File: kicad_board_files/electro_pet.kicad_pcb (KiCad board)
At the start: 2 copper layers, 42 x 63.8 mm, 20 parts, among them M3_bolt_nut_custom VAL**, SW1 SWITCH_INV, SW2 SW_PUSH, SW3 SW_PUSH, U1 8X8_LED_MATRIX, U2 LIPO_CHARGER, U3 ELECTRO_HAT, U4 V_REG, U5 MPU-6050, U6 DC_DC_BOOST, U7 ARDUINO_PRO_MICRO, U8 BATTERY_CUSTOM, U9 A3144

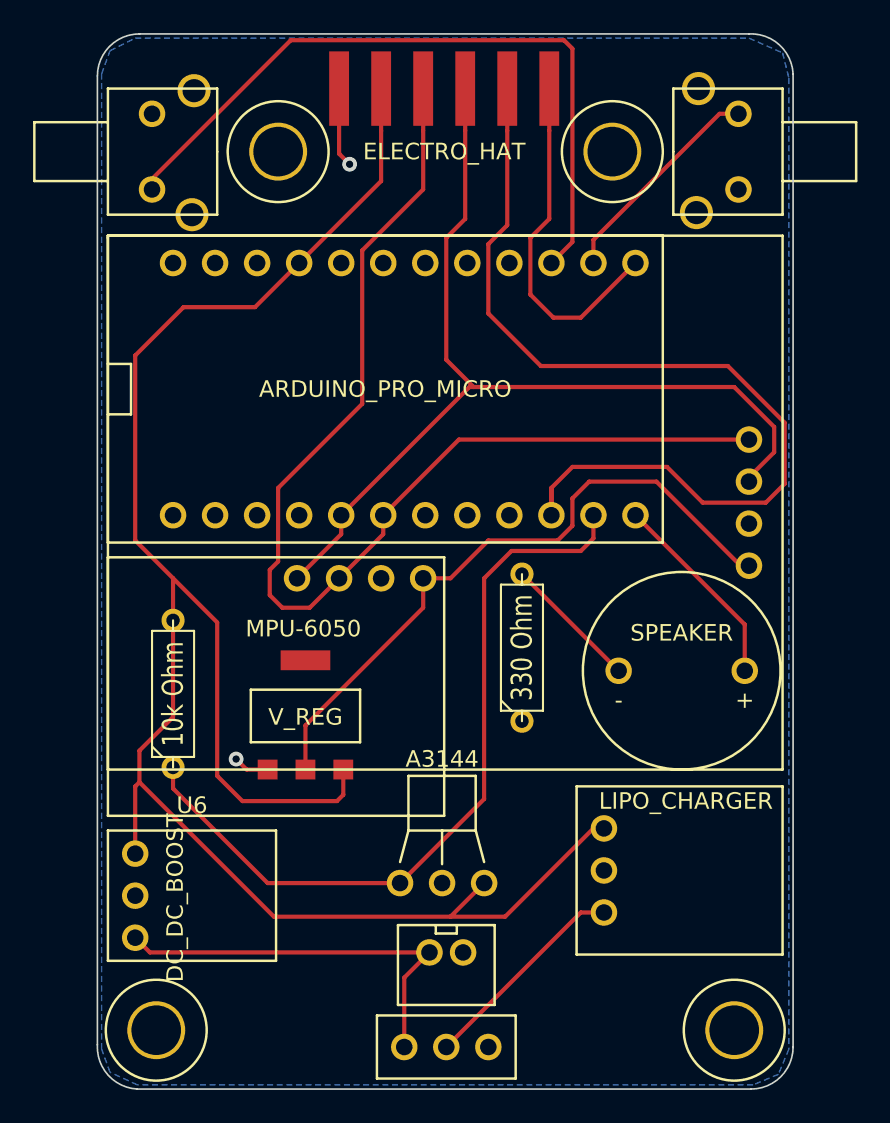
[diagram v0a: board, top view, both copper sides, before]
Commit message: fixed a wiring issue with the switch
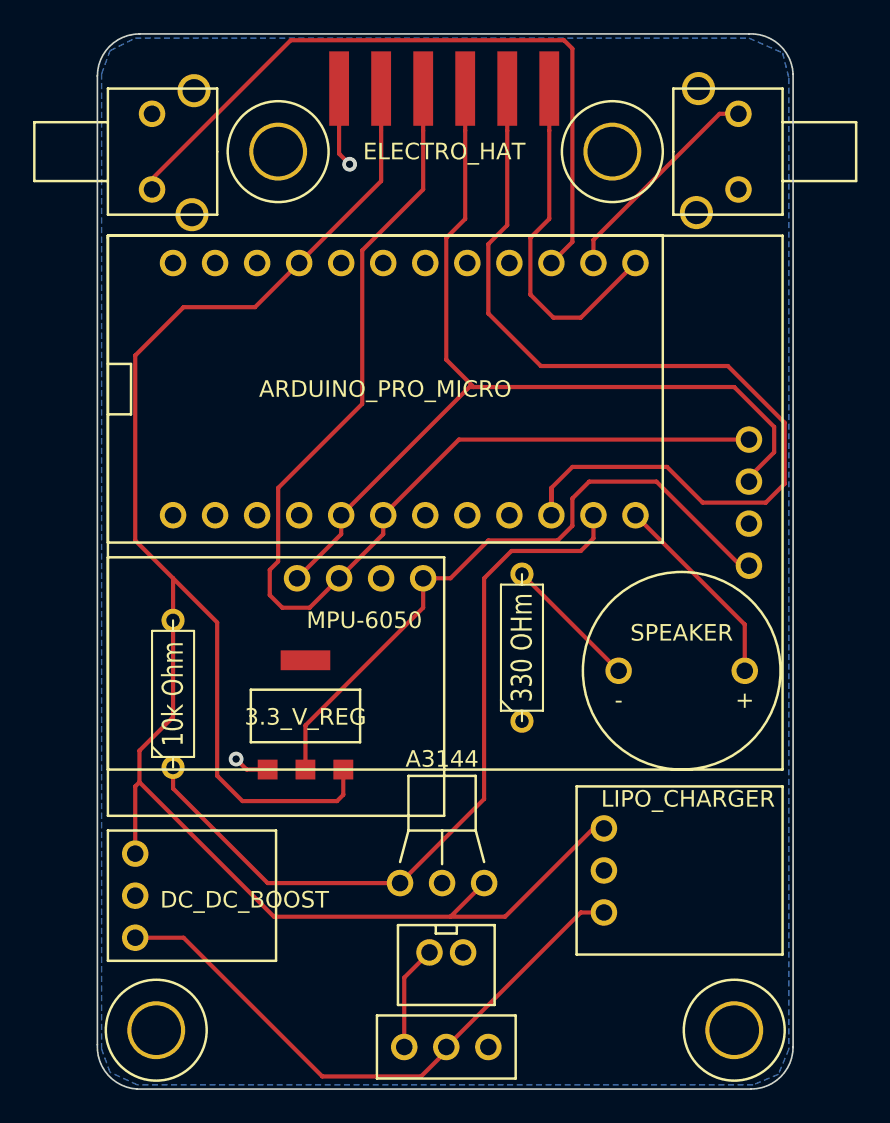
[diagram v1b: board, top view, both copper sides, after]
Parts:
- removed 330 Ohm: R, R3-5
- added 330 OHm: R, R3-5, F.Cu at (306.8, 79.4)
- U4: value V_REG -> 3.3_V_REG
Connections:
- SW1 pad 1: N-0000012 -> N-0000010
- U6 pad 3: N-0000012 -> N-0000026
- U8 pad 2: N-0000012 -> N-0000010
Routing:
- net N-0000012: track 24.5 -> 0.00 mm
- net N-0000026: track 12.9 -> 36.0 mm
- net N-0000010: track 0.00 -> 6.35 mm
